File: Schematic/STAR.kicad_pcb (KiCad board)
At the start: 2 copper layers, 54 parts, among them J1 796739-2, J14 Conn_02x20_Odd_Even, J15 Conn_02x20_Odd_Even, J3 Conn_01x04, J4 SMB, U1 1043, U12 TLV75533PDBV, U16 BQ25798RQMR, U18 DRV8243SQDGQRQ1 (S-Variant), U19 DRV8243SQDGQRQ1 (S-Variant), U2 1043, U20 LS7366R-S, U21 LS7366R-S, U28 TPS566238PRQFR, U29 TPS40305DRCT, U3 1043, U4 1043, U5 1043, U6 1043, U8 BQ7692000PWR, Y1 ASV-30.000MHZ-E-T

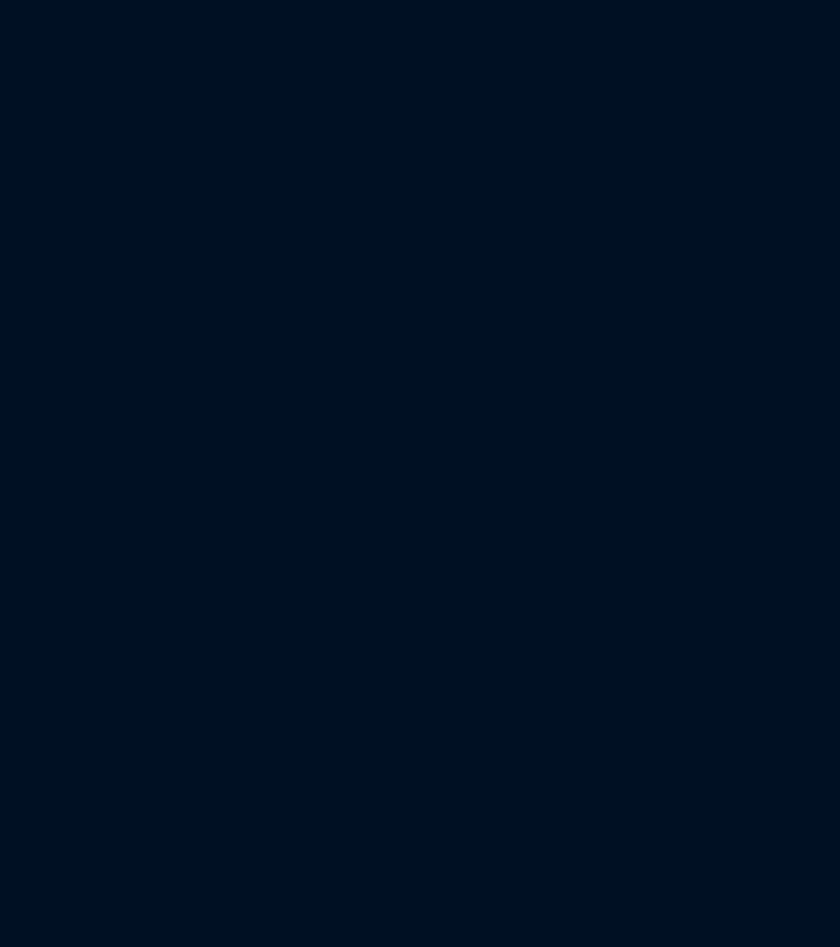
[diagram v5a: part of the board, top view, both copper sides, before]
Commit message: 100n cap
100n cap bom
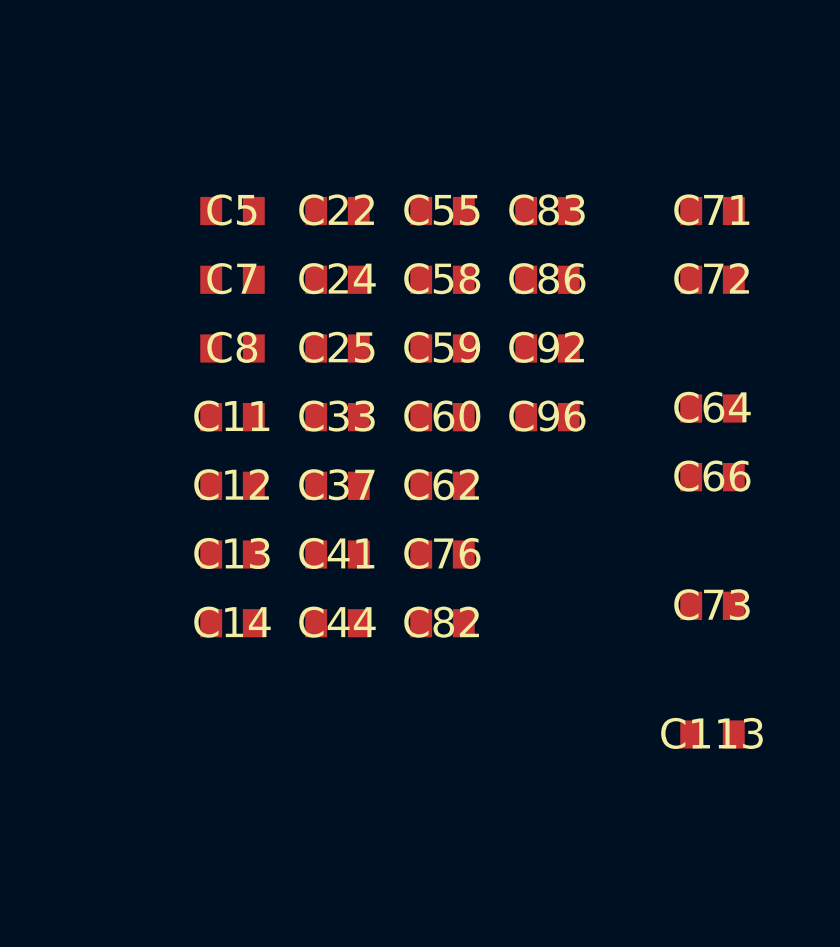
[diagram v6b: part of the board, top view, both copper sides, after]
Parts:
- added C11: 100n, CL10B104MB8NNNC:CAPC1608X90N, F.Cu at (458.8, 95.4)
- added C113: 100n, CL10B104MB8NNNC:CAPC1608X90N, F.Cu at (474.8, 106.0)
- added C12: 100n, CL10B104MB8NNNC:CAPC1608X90N, F.Cu at (458.8, 97.7)
- added C13: 100n, CL10B104MB8NNNC:CAPC1608X90N, F.Cu at (458.8, 100.0)
- added C14: 100n, CL10B104MB8NNNC:CAPC1608X90N, F.Cu at (458.8, 102.3)
- added C22: 100n, CL10B104MB8NNNC:CAPC1608X90N, F.Cu at (462.3, 88.5)
- added C24: 100n, CL10B104MB8NNNC:CAPC1608X90N, F.Cu at (462.3, 90.8)
- added C25: 100n, CL10B104MB8NNNC:CAPC1608X90N, F.Cu at (462.3, 93.1)
- added C33: 100n, CL10B104MB8NNNC:CAPC1608X90N, F.Cu at (462.3, 95.4)
- added C37: 100n, CL10B104MB8NNNC:CAPC1608X90N, F.Cu at (462.3, 97.7)
- added C41: 100n, CL10B104MB8NNNC:CAPC1608X90N, F.Cu at (462.3, 100.0)
- added C44: 100n, CL10B104MB8NNNC:CAPC1608X90N, F.Cu at (462.3, 102.3)
- added C5: 100n, CL10B104MB8NNNC:CAPC1608X90N, F.Cu at (458.8, 88.5)
- added C55: 100n, CL10B104MB8NNNC:CAPC1608X90N, F.Cu at (465.8, 88.5)
- added C58: 100n, CL10B104MB8NNNC:CAPC1608X90N, F.Cu at (465.8, 90.8)
- added C59: 100n, CL10B104MB8NNNC:CAPC1608X90N, F.Cu at (465.8, 93.1)
- added C60: 100n, CL10B104MB8NNNC:CAPC1608X90N, F.Cu at (465.8, 95.4)
- added C62: 100n, CL10B104MB8NNNC:CAPC1608X90N, F.Cu at (465.8, 97.7)
- added C64: 100n, CL10B104MB8NNNC:CAPC1608X90N, F.Cu at (474.8, 95.1)
- added C66: 100n, CL10B104MB8NNNC:CAPC1608X90N, F.Cu at (474.8, 97.4)
- added C7: 100n, CL10B104MB8NNNC:CAPC1608X90N, F.Cu at (458.8, 90.8)
- added C71: 100n, CL10B104MB8NNNC:CAPC1608X90N, F.Cu at (474.8, 88.5)
- added C72: 100n, CL10B104MB8NNNC:CAPC1608X90N, F.Cu at (474.8, 90.8)
- added C73: 100n, CL10B104MB8NNNC:CAPC1608X90N, F.Cu at (474.8, 101.7)
- added C76: 100n, CL10B104MB8NNNC:CAPC1608X90N, F.Cu at (465.8, 100.0)
- added C8: 100n, CL10B104MB8NNNC:CAPC1608X90N, F.Cu at (458.8, 93.1)
- added C82: 100n, CL10B104MB8NNNC:CAPC1608X90N, F.Cu at (465.8, 102.3)
- added C83: 100n, CL10B104MB8NNNC:CAPC1608X90N, F.Cu at (469.3, 88.5)
- added C86: 100n, CL10B104MB8NNNC:CAPC1608X90N, F.Cu at (469.3, 90.8)
- added C92: 100n, CL10B104MB8NNNC:CAPC1608X90N, F.Cu at (469.3, 93.1)
- added C96: 100n, CL10B104MB8NNNC:CAPC1608X90N, F.Cu at (469.3, 95.4)

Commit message: added test points and fet
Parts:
- removed C11, C113, C22, C24, C25, C33, C37, C44, C58, C59, C60, C62, C64, C66, C7, C73, C76, C8, C82, C83, C86, C92, C96: 100n, CL10B104MB8NNNC:CAPC1608X90N
- removed J14: Conn_02x20_Odd_Even, 7-534206-0:SHDR40W69P254_2X20_5080X503X813P
- removed J15: Conn_02x20_Odd_Even, Connector_PinHeader_2.54mm:PinHeader_2x20_P2.54mm_Vertical
- removed U1, U2, U3, U4, U5, U6: 1043, 1043:1043
- removed U16: BQ25798RQMR, BQ25798RQMR:BQ25798RQMR
- removed U18, U19: DRV8243SQDGQRQ1 (S-Variant), DRV8243SQDGQRQ1:SOP50P490X110-29N
- removed U20: LS7366R-S, LS7366R_S:SOIC127P600X175-14N
- added C1: 100n, Capacitor_SMD:C_0603_1608Metric_Pad1.08x0.95mm_HandSolder, F.Cu at (305.2, 210.4)
- added C109: 100n, Capacitor_SMD:C_0603_1608Metric_Pad1.08x0.95mm_HandSolder, F.Cu at (324.6, 229.0)
- added C119: 100n, Capacitor_SMD:C_0603_1608Metric_Pad1.08x0.95mm_HandSolder, F.Cu at (324.6, 217.5)
- added C121: 100n, Capacitor_SMD:C_0603_1608Metric_Pad1.08x0.95mm_HandSolder, F.Cu at (324.6, 220.0)
- added C126: 100n, Capacitor_SMD:C_0603_1608Metric_Pad1.08x0.95mm_HandSolder, F.Cu at (324.6, 210.4)
- added C127: 100n, Capacitor_SMD:C_0603_1608Metric_Pad1.08x0.95mm_HandSolder, F.Cu at (324.6, 213.0)
- added C128: 100n, Capacitor_SMD:C_0603_1608Metric_Pad1.08x0.95mm_HandSolder, F.Cu at (324.6, 224.5)
- added C15: 100n, Capacitor_SMD:C_0603_1608Metric_Pad1.08x0.95mm_HandSolder, F.Cu at (305.2, 223.0)
- added C16: 100n, Capacitor_SMD:C_0603_1608Metric_Pad1.08x0.95mm_HandSolder, F.Cu at (305.2, 225.5)
- added C19: 100n, Capacitor_SMD:C_0603_1608Metric_Pad1.08x0.95mm_HandSolder, F.Cu at (309.6, 210.4)
- added C28: 100n, Capacitor_SMD:C_0603_1608Metric_Pad1.08x0.95mm_HandSolder, F.Cu at (309.6, 213.0)
- added C30: 100n, Capacitor_SMD:C_0603_1608Metric_Pad1.08x0.95mm_HandSolder, F.Cu at (309.6, 215.5)
- added C31: 100n, Capacitor_SMD:C_0603_1608Metric_Pad1.08x0.95mm_HandSolder, F.Cu at (309.6, 218.0)
- added C36: 100n, Capacitor_SMD:C_0603_1608Metric_Pad1.08x0.95mm_HandSolder, F.Cu at (309.6, 220.5)
- added C38: 100n, Capacitor_SMD:C_0603_1608Metric_Pad1.08x0.95mm_HandSolder, F.Cu at (309.6, 223.0)
- added C54: 100n, Capacitor_SMD:C_0603_1608Metric_Pad1.08x0.95mm_HandSolder, F.Cu at (313.9, 210.4)
- added C56: 100n, Capacitor_SMD:C_0603_1608Metric_Pad1.08x0.95mm_HandSolder, F.Cu at (313.9, 215.5)
- added C65: 100n, Capacitor_SMD:C_0603_1608Metric_Pad1.08x0.95mm_HandSolder, F.Cu at (313.9, 218.0)
- added C67: 100n, Capacitor_SMD:C_0603_1608Metric_Pad1.08x0.95mm_HandSolder, F.Cu at (313.9, 220.5)
- added C69: 100n, Capacitor_SMD:C_0603_1608Metric_Pad1.08x0.95mm_HandSolder, F.Cu at (313.9, 223.0)
- added C75: 100n, Capacitor_SMD:C_0603_1608Metric_Pad1.08x0.95mm_HandSolder, F.Cu at (318.3, 213.0)
- added C81: 100n, Capacitor_SMD:C_0603_1608Metric_Pad1.08x0.95mm_HandSolder, F.Cu at (318.3, 215.5)
- added C85: 100n, Capacitor_SMD:C_0603_1608Metric_Pad1.08x0.95mm_HandSolder, F.Cu at (318.3, 218.0)
- added J10: Optical Encoder 1, Connector_PinHeader_2.54mm:PinHeader_1x06_P2.54mm_Vertical, F.Cu at (318.4, 134.8)
- added J11: 796739-2, 796739-2:7967392, F.Cu at (300.3, 154.2)
- added J13: Optical Encoder 2, Connector_PinHeader_2.54mm:PinHeader_1x06_P2.54mm_Vertical, F.Cu at (323.0, 134.8)
- added J2: 796739-2, 796739-2:7967392, F.Cu at (291.6, 172.0)
- added J5: Conn_02x20_Odd_Even, Connector_PinHeader_2.54mm:PinHeader_2x20_P2.54mm_Vertical, F.Cu at (287.6, 113.3)
- added J9: 796739-2, 796739-2:7967392, F.Cu at (300.3, 138.6)
- added Q15: CSD19531Q5AT, CSD19531Q5AT:CSD19531Q5AT, F.Cu at (330.3, 169.8)
- added Q16: CSD19531Q5AT, CSD19531Q5AT:CSD19531Q5AT, F.Cu at (330.3, 177.8)
- added Q4: CSD19531Q5AT, CSD19531Q5AT:CSD19531Q5AT, F.Cu at (271.6, 108.4)
- added Q5: CSD19531Q5AT, CSD19531Q5AT:CSD19531Q5AT, F.Cu at (271.6, 116.4)
- added Q7: CSD19531Q5AT, CSD19531Q5AT:CSD19531Q5AT, F.Cu at (271.6, 124.3)
- added Q8: CSD19531Q5AT, CSD19531Q5AT:CSD19531Q5AT, F.Cu at (271.6, 132.3)
- added TH1: NTCGS163JX103DT7, NTCGS163JX103DT7:THRMC1608X90N, F.Cu at (309.6, 190.4)
- added TH2: NTCGS163JX103DT7, NTCGS163JX103DT7:THRMC1608X90N, F.Cu at (309.6, 193.0)
- added TP1: TestPoint, 5017:5017, F.Cu at (367.1, 195.3)
- added TP10: TestPoint, 5017:5017, F.Cu at (380.0, 200.2)
- added TP11: TestPoint, 5017:5017, F.Cu at (380.0, 205.0)
- added TP12: TestPoint, 5017:5017, F.Cu at (339.3, 169.1)
- added TP13: TestPoint, 5017:5017, F.Cu at (339.3, 173.9)
- added TP14: TestPoint, 5017:5017, F.Cu at (339.3, 178.8)
- added TP15: TestPoint, 5017:5017, F.Cu at (339.3, 183.6)
- added TP16: TestPoint, 5017:5017, F.Cu at (339.3, 188.4)
- added TP17: TestPoint, 5017:5017, F.Cu at (339.3, 193.3)
- added TP18: TestPoint, 5017:5017, F.Cu at (339.3, 198.2)
- added TP19: TestPoint, 5017:5017, F.Cu at (345.8, 169.1)
- added TP2: TestPoint, 5017:5017, F.Cu at (367.1, 200.2)
- added TP20: TestPoint, 5017:5017, F.Cu at (345.8, 173.9)
- added TP21: TestPoint, 5017:5017, F.Cu at (345.8, 178.8)
- added TP22: TestPoint, 5017:5017, F.Cu at (345.8, 183.6)
- added TP23: TestPoint, 5017:5017, F.Cu at (345.8, 188.4)
- added TP24: TestPoint, 5017:5017, F.Cu at (345.8, 193.3)
- added TP25: TestPoint, 5017:5017, F.Cu at (345.8, 198.2)
- added TP26: TestPoint, 5017:5017, F.Cu at (352.2, 169.1)
- added TP27: TestPoint, 5017:5017, F.Cu at (352.2, 173.9)
- added TP28: TestPoint, 5017:5017, F.Cu at (352.2, 178.8)
- added TP29: TestPoint, 5017:5017, F.Cu at (352.2, 183.6)
- added TP3: TestPoint, 5017:5017, F.Cu at (367.1, 205.0)
- added TP30: TestPoint, 5017:5017, F.Cu at (352.2, 188.4)
- added TP31: TestPoint, 5017:5017, F.Cu at (352.2, 193.3)
- added TP32: TestPoint, 5017:5017, F.Cu at (352.2, 198.2)
- added TP33: TestPoint, 5017:5017, F.Cu at (358.6, 169.1)
- added TP34: TestPoint, 5017:5017, F.Cu at (358.6, 173.9)
- added TP35: TestPoint, 5017:5017, F.Cu at (358.6, 178.8)
- added TP36: TestPoint, 5017:5017, F.Cu at (358.6, 183.6)
- added TP37: TestPoint, 5017:5017, F.Cu at (358.6, 188.4)
- added TP38: TestPoint, 5017:5017, F.Cu at (358.6, 193.3)
- added TP39: TestPoint, 5017:5017, F.Cu at (367.1, 169.1)
- added TP4: TestPoint, 5017:5017, F.Cu at (367.1, 209.8)
- added TP40: TestPoint, 5017:5017, F.Cu at (367.1, 173.9)
- added TP41: TestPoint, 5017:5017, F.Cu at (367.1, 178.8)
- added TP42: TestPoint, 5017:5017, F.Cu at (367.1, 183.6)
- added TP43: TestPoint, 5017:5017, F.Cu at (367.1, 188.4)
- added TP44: TestPoint, 5017:5017, F.Cu at (373.6, 169.1)
- added TP45: TestPoint, 5017:5017, F.Cu at (373.6, 173.9)
- added TP46: TestPoint, 5017:5017, F.Cu at (373.6, 178.8)
- added TP47: TestPoint, 5017:5017, F.Cu at (373.6, 183.6)
- added TP48: TestPoint, 5017:5017, F.Cu at (373.6, 188.4)
- added TP49: TestPoint, 5017:5017, F.Cu at (380.0, 169.1)
- added TP5: TestPoint, 5017:5017, F.Cu at (373.6, 195.3)
- added TP50: TestPoint, 5017:5017, F.Cu at (380.0, 173.9)
- added TP51: TestPoint, 5017:5017, F.Cu at (380.0, 178.8)
- added TP52: TestPoint, 5017:5017, F.Cu at (339.3, 205.0)
- added TP53: TestPoint, 5017:5017, F.Cu at (339.3, 209.8)
- added TP6: TestPoint, 5017:5017, F.Cu at (373.6, 200.2)
- added TP7: TestPoint, 5017:5017, F.Cu at (373.6, 205.0)
- added TP8: TestPoint, 5017:5017, F.Cu at (373.6, 209.8)
- added TP9: TestPoint, 5017:5017, F.Cu at (380.0, 195.3)
- added U10: 1043, 1043:1043, F.Cu at (262.8, 164.7)
- added U11: 1043, 1043:1043, F.Cu at (262.8, 188.8)
- added U13: 1043, 1043:1043, F.Cu at (262.8, 237.1)
- added U15: BQ7692000PWR, Package_SO:TSSOP-20_4.4x6.5mm_P0.65mm, F.Cu at (271.4, 200.3)
- added U17: TLV75533PDBV, Package_TO_SOT_SMD:SOT-23-5, F.Cu at (280.3, 212.8)
- added U23: BQ25798RQMR, BQ25798RQMR:BQ25798RQMR, F.Cu at (279.5, 200.0)
- added U24: TPS40305DRCT, TPS40305DRCT:TPS40305DRCT, F.Cu at (328.6, 185.0)
- added U25: 74LVC125APW_118, 74LVC125APW,118:SOP65P640X110-14N, F.Cu at (289.7, 240.3)
- added U26: DRV8243SQDGQRQ1 (S-Variant), DRV8243SQDGQRQ1:SOP50P490X110-29N, F.Cu at (289.0, 221.5)
- added U27: DRV8243SQDGQRQ1 (S-Variant), DRV8243SQDGQRQ1:SOP50P490X110-29N, F.Cu at (296.4, 221.5)
- added U9: 1043, 1043:1043, F.Cu at (262.8, 140.6)
- C12, C13, C14, C41, C5, C55, C71, C72: footprint CL10B104MB8NNNC:CAPC1608X90N -> Capacitor_SMD:C_0603_1608Metric_Pad1.08x0.95mm_HandSolder
- D21: value RED -> GREEN
- D26: value GREEN -> 5V6; footprint ASMM-CR03-BU802:LEDM3528X210N -> DDZ5V6ASF-7:SODFL2512X75N
- D28: value 5V6 -> RED; footprint DDZ5V6ASF-7:SODFL2512X75N -> ASMM-CR03-BU802:LEDM3528X210N
- J1: value 796739-2 -> Conn_01x04; footprint 796739-2:7967392 -> Connector_PinHeader_2.54mm:PinHeader_1x04_P2.54mm_Vertical
- J3: value Conn_01x04 -> SMB
- J4: value SMB -> Conn_02x20_Odd_Even; footprint Connector_PinHeader_2.54mm:PinHeader_1x04_P2.54mm_Vertical -> 7-534206-0:SHDR40W69P254_2X20_5080X503X813P
- U12: value TLV75533PDBV -> 1043; footprint Package_TO_SOT_SMD:SOT-23-5 -> 1043:1043
- U21: value LS7366R-S -> TPS566238PRQFR; footprint LS7366R_S:SOIC127P600X175-14N -> TPS566238PRQFR:TPS566238PRQFR
- U28: value TPS566238PRQFR -> LS7366R-S; footprint TPS566238PRQFR:TPS566238PRQFR -> LS7366R_S:SOIC127P600X175-14N
- U29: value TPS40305DRCT -> LS7366R-S; footprint TPS40305DRCT:TPS40305DRCT -> LS7366R_S:SOIC127P600X175-14N
- U8: value BQ7692000PWR -> 1043; footprint Package_SO:TSSOP-20_4.4x6.5mm_P0.65mm -> 1043:1043
- moved C71 211.3 mm to (313.9, 225.5)
- moved C41 197.7 mm to (309.6, 225.5)
- moved C5 197.6 mm to (305.2, 213.0)
- moved C72 197.0 mm to (318.3, 210.4)
- moved C55 196.3 mm to (313.9, 213.0)
- moved C14 193.8 mm to (305.2, 220.5)
- moved C13 193.6 mm to (305.2, 218.0)
- moved C12 193.5 mm to (305.2, 215.5)
- moved U29 60.3 mm to (298.7, 200.7)
- moved D26 56.1 mm to (268.9, 182.8)
- moved U8 53.8 mm to (262.8, 116.5)
- moved J4 50.2 mm to (287.3, 109.0)
- moved U21 39.9 mm to (275.0, 212.9)
- moved J1 36.6 mm to (287.6, 183.7)
- moved D29 34.3 mm to (288.4, 228.1)
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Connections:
- C12 pad 1: /BMS Protection Board/LDO_3V3 -> /BMS Protection Board/LDO_1V5
- C13 pad 1: Net-(C13-Pad1) -> GND
- C13 pad 2: /PACK+ -> /BMS Protection Board/SRP
- C14 pad 1: /BMS Protection Board/SRN -> /BATT+
- C14 pad 2: GND -> Net-(C14-Pad2)
- C55 pad 1: /BMS Protection Board/REGOUT -> /P5V0
- C71 pad 1: /Motor Control Board/P6V0 -> Net-(U21-SW)
- C71 pad 2: GND -> Net-(U21-BST)
- C72 pad 1: /Motor Control Board/P6V0 -> /PACK+
- D21 pad 1: /BMS Protection Board/STAT_1_2 -> Net-(U19-LED1)
- D21 pad 2: Net-(D21-Pad2) -> Net-(Q14-E)
- D26 pad 2: Net-(Q14-E) -> GND
- D28 pad 1: Net-(D28-K) -> /BMS Protection Board/STAT_1_2
- D28 pad 2: GND -> Net-(D28-Pad2)
- J1 pad 1: /BATT+ -> /C0
- J1 pad 2: /BATT- -> /C1
- J3 pad 1: /C0 -> GND
- J3 pad 2: /C1 -> /SMBC
- J3 pad 3: /C2 -> /SMBD
- J3 pad 4: /C3 -> unconnected-(J3-Pin_4-Pad4)
- J4 pad 1: GND -> /MCU_P3V3
- J4 pad 2: /SMBC -> /MCU/5V
- J4 pad 3: /SMBD -> /MCU/SDA
- J4 pad 4: unconnected-(J4-Pin_4-Pad4) -> /MCU/5V
- L1 pad 2: Net-(U28-SW) -> Net-(U21-SW)
- L3 pad 1: Net-(Q16-D) -> Net-(U24-SW)
- U12 pad 1: /P5V0 -> /C2
- U12 pad 2: GND -> /C1
- U21 pad 1: unconnected-(U21-FCKO-Pad1) -> Net-(U21-VCC)
- U21 pad 2: /Motor Control Board/Quadrature Counter/FCKI -> Net-(U21-FB)
- U21 pad 3: GND -> unconnected-(U21-EN-Pad3)
- U21 pad 4: /ENCODER2_nCS -> GND
- U21 pad 5: /SPI_SCLK -> /PACK+
- U21 pad 6: /SPI_SDO -> /PACK+
- U21 pad 7: /SPI_SDI -> Net-(U21-BST)
- U21 pad 8: /ENCODER2_LFLAG/ -> Net-(U21-SW)
- U21 pad 9: unconnected-(U21-DFLAG/-Pad9) -> Net-(U21-PG)
- U28 pad 1: Net-(U28-VCC) -> unconnected-(U28-FCKO-Pad1)
- U28 pad 2: Net-(U28-FB) -> /Motor Control Board/Quadrature Counter/FCKI
- U28 pad 3: unconnected-(U28-EN-Pad3) -> GND
- U28 pad 4: GND -> /ENCODER1_nCS
- U28 pad 5: /PACK+ -> /SPI_SCLK
- U28 pad 6: /PACK+ -> /SPI_SDO
- U28 pad 7: Net-(U28-BST) -> /SPI_SDI
- U28 pad 8: Net-(U28-SW) -> /ENCODER1_LFLAG/
- U28 pad 9: Net-(U28-PG) -> unconnected-(U28-DFLAG/-Pad9)
- U29 pad 1: /Motor Control Board/Motor 6V Line/PACK+ -> unconnected-(U29-FCKO-Pad1)
- U29 pad 10: Net-(U29-BP) -> /MCU_P3V3
- U29 pad 11: GND -> /Motor Control Board/ENCODER2_OUTPUT2
- U29 pad 12: GND -> /Motor Control Board/ENCODER2_OUTPUT1
- U29 pad 13: GND -> /MCU_P3V3
- U29 pad 14: GND -> /MCU_P3V3
- U29 pad 2: Net-(U29-EN/SS) -> /Motor Control Board/Quadrature Counter/FCKI
- U29 pad 3: Net-(U29-PGOOD) -> GND
- U29 pad 4: Net-(U29-COMP) -> /ENCODER2_nCS
- U29 pad 5: Net-(U29-FB) -> /SPI_SCLK
- U29 pad 6: Net-(U29-BOOT) -> /SPI_SDO
- U29 pad 7: Net-(Q15-G) -> /SPI_SDI
- U29 pad 8: Net-(Q16-D) -> /ENCODER2_LFLAG/
- U29 pad 9: Net-(Q16-G) -> unconnected-(U29-DFLAG/-Pad9)
- U8 pad 1: /BMS Protection Board/DSG_EN -> /C3
- U8 pad 2: /BMS Protection Board/CHG_EN -> /C2

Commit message: usb-c
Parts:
- added J12: SS-52400-002, SS-52400-002:SS52400002, F.Cu at (347.3, 111.2)
- TP1, TP10, TP11, TP12, TP13, TP14, TP16, TP17, TP18, TP19, TP2, TP20, TP21, TP22, TP23, TP24, TP25, TP26, TP27, TP28, TP29, TP3, TP30, TP31, TP32, TP33, TP34, TP35, TP36, TP37, TP38, TP39, TP4, TP40, TP41, TP42, TP43, TP44, TP45, TP46, TP47, TP48, TP49, TP5, TP50, TP51, TP52, TP53, TP6, TP7: footprint 5017:5017 -> 3825:3825
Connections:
- D18 pad 1: /BMS Protection Board/USB_C_N -> /BMS Protection Board/USB_C_P
- D19 pad 1: /BMS Protection Board/USB_C_P -> /BMS Protection Board/USB_C_N
- TP22 pad 1: /BMS Protection Board/VC5 -> /BMS Protection Board/VC3
